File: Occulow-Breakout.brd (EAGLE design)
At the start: 50.8 x 50.8 mm, 18 parts

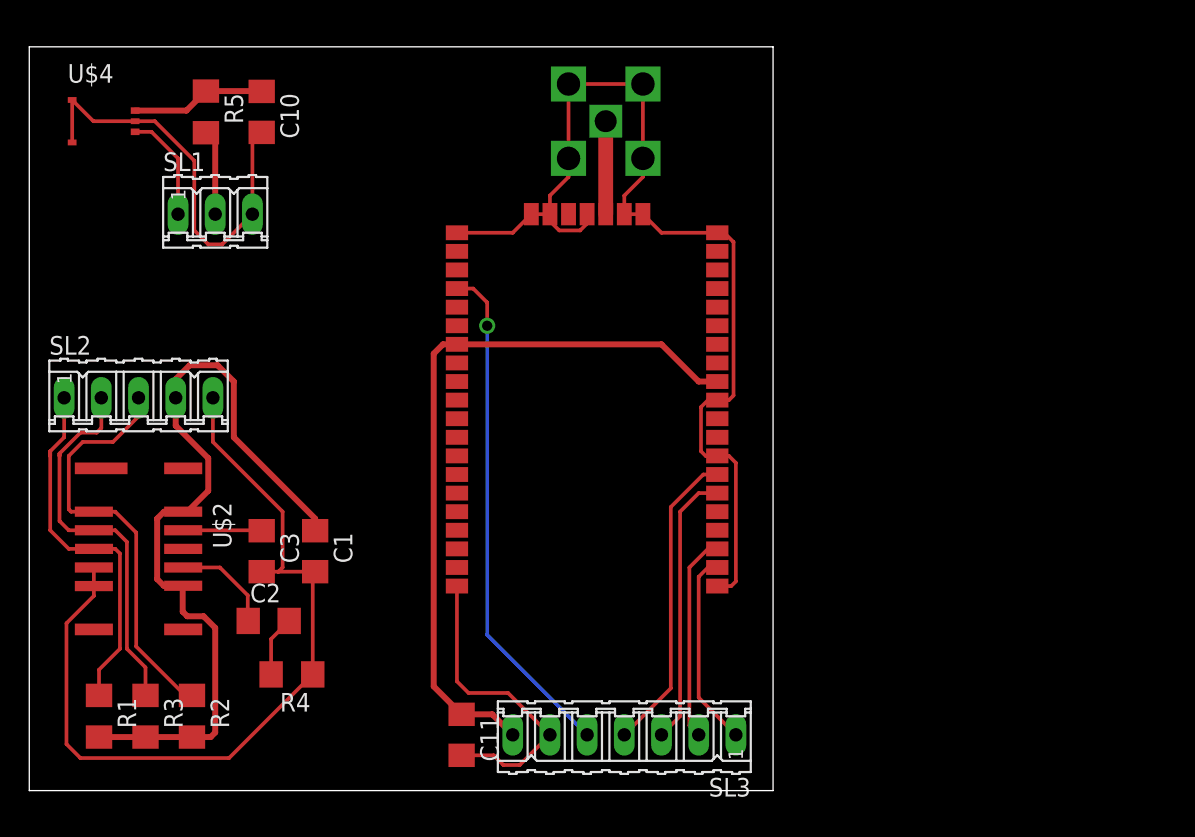
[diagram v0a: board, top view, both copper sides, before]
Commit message: Re-named ground for each module
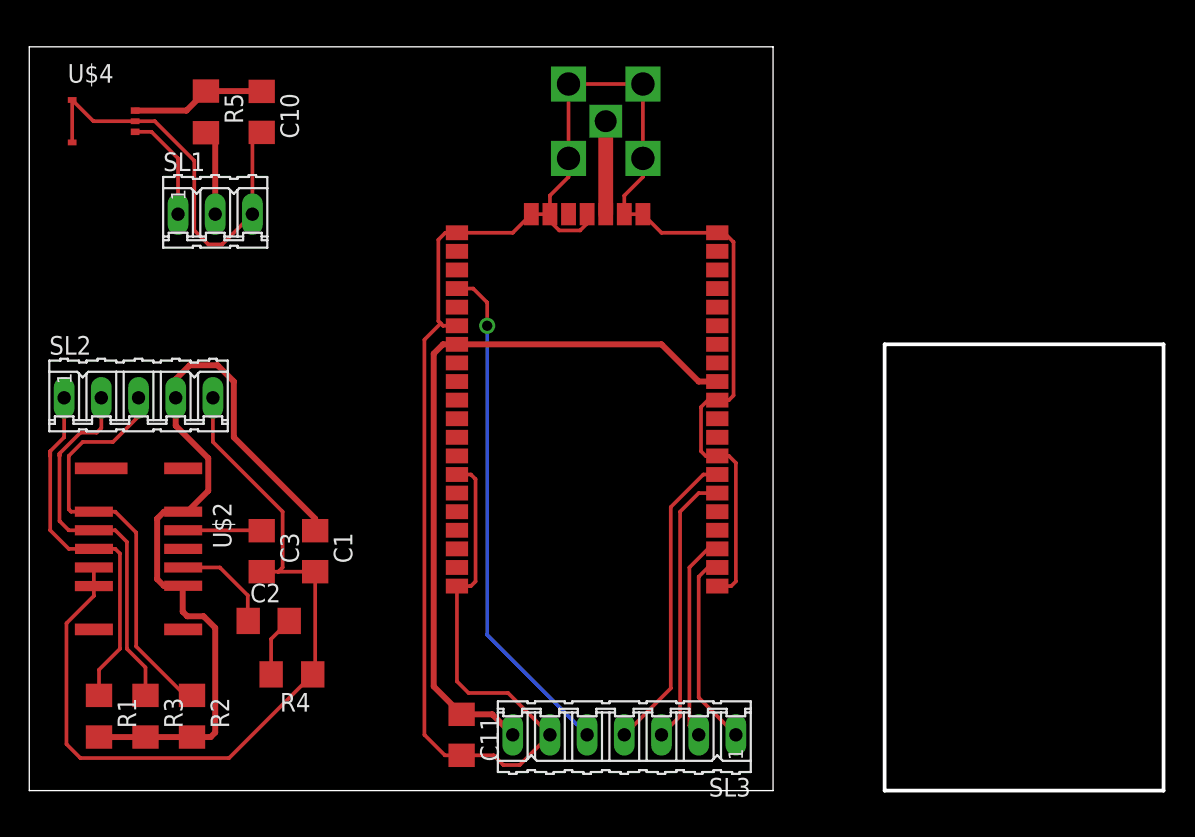
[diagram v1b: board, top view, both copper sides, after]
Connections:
- removed net GND: C1.2, C10.2, C11.2, C3.2, R4.1, SL1.3, SL2.5, SL3.6, U$1.1, U$1.11, U$1.20, U$1.21, U$1.22, U$1.24, U$1.26, U$1.27, U$1.28, U$1.33, U$1.41, U$1.47, U$1.8, U$2.5, U$2.6, U$3.1, U$3.2, U$3.3, U$3.4, U$4.2, U$4.4, U$4.5
- new net GR_GND: C1.2, C3.2, R4.1, SL2.5, U$2.5, U$2.6
- new net LR_GND: C11.2, SL3.6, U$1.1, U$1.11, U$1.20, U$1.21, U$1.22, U$1.24, U$1.26, U$1.27, U$1.28, U$1.33, U$1.41, U$1.47, U$1.8, U$3.1, U$3.2, U$3.3, U$3.4
- new net PIR_GND: C10.2, SL1.3, U$4.2, U$4.4, U$4.5
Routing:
- net GND: track 178.9 -> 0.00 mm
- net LR_GND: track 0.00 -> 142.8 mm
- net GR_GND: track 0.00 -> 57.4 mm
- net PIR_GND: track 0.00 -> 28.8 mm
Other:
- board size 50.8 x 50.8 mm -> 77.5 x 50.8 mm

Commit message: Panelized layout
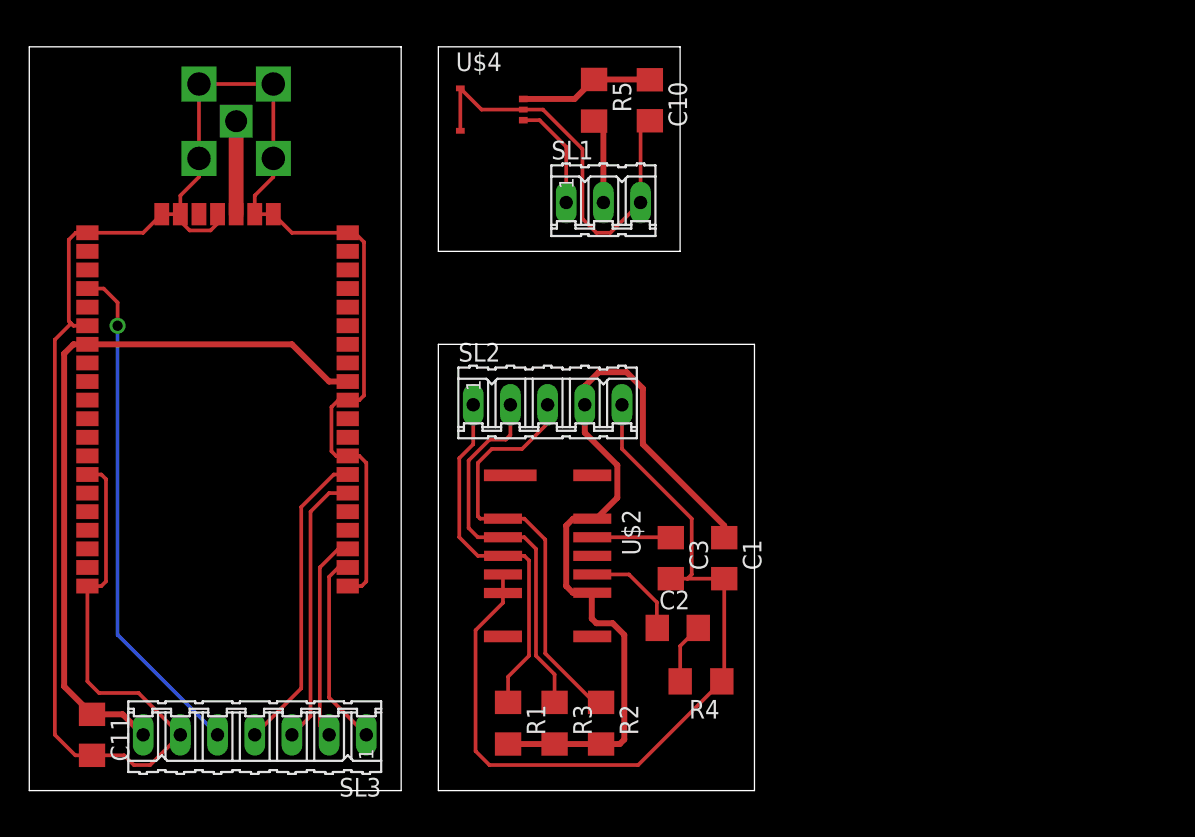
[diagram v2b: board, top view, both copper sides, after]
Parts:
- moved C1 27.9 mm to (47.5, 15.9)
- moved R1 27.9 mm to (32.7, 4.60)
- moved R2 27.9 mm to (39.1, 4.60)
- moved C2 27.9 mm to (44.3, 11.1)
- moved C3 27.9 mm to (43.8, 15.9)
- moved R3 27.9 mm to (35.9, 4.60)
- moved R4 27.9 mm to (45.9, 7.46)
- moved SL2 27.9 mm to (35.4, 26.4)
- moved U$2 27.9 mm to (35.4, 16.0)
- moved R5 26.5 mm to (38.6, 47.1)
- moved SL1 26.5 mm to (39.2, 40.2)
- moved C10 26.5 mm to (42.4, 47.1)
- moved U$4 26.5 mm to (31.6, 46.5)
- moved C11 25.2 mm to (4.29, 3.81)
- moved SL3 25.2 mm to (15.4, 3.81)
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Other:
- board size 77.5 x 50.8 mm -> 49.5 x 50.8 mm

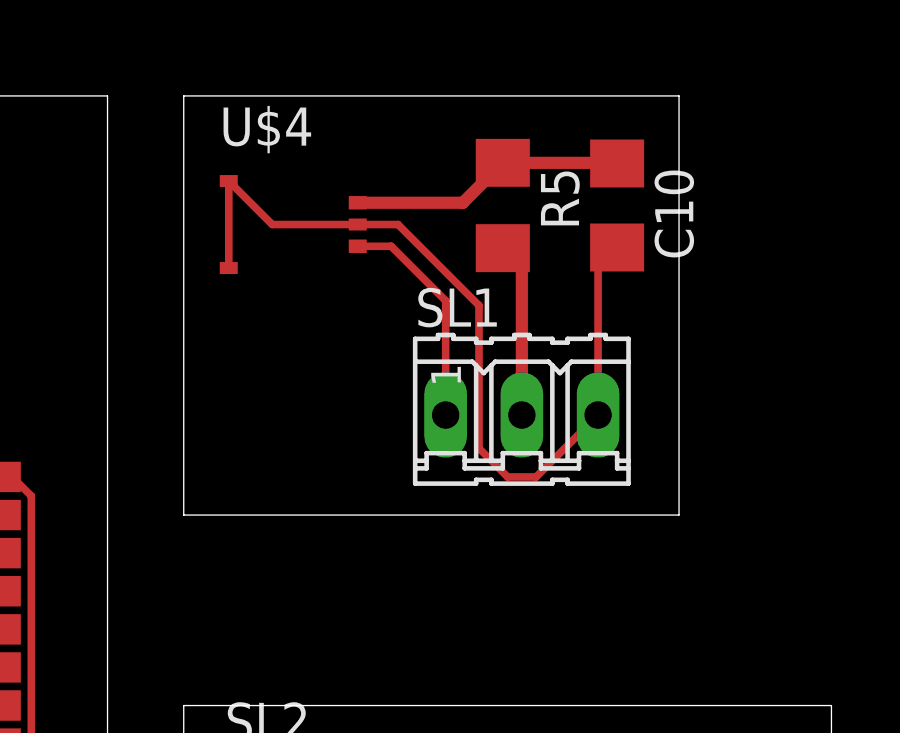
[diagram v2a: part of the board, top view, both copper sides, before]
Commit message: Labels for PIR header, rearranged
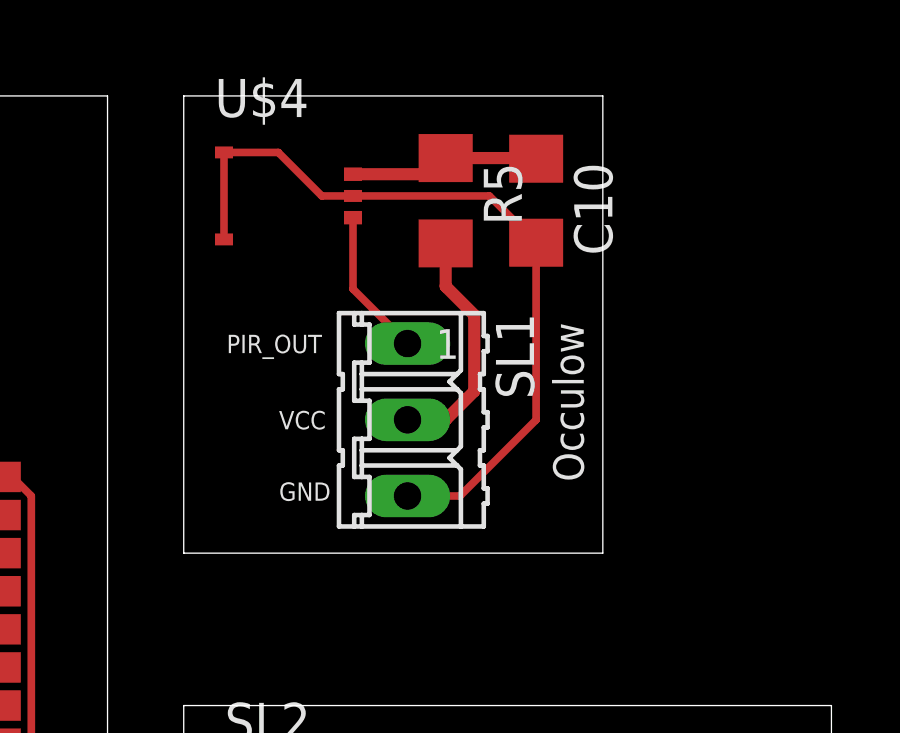
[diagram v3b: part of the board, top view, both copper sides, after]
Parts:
- moved SL1 3.81 mm to (35.4, 40.0), turned to 270 degrees
- moved C10 2.70 mm to (39.7, 47.3)
- moved R5 1.91 mm to (36.7, 47.3)
- moved U$4 0.97 mm to (31.4, 47.5)
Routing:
- net PIR_GND: track 28.8 -> 25.8 mm
- net N$5: track 9.21 -> 6.34 mm
- net PIR_OUT: track 7.49 -> 4.95 mm
- net PIR_VCC: track 5.83 -> 7.94 mm
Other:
- outline, holes or cut-outs redrawn
- board text added: "GND"
- board text added: "Occulow"
- board text added: "PIR_OUT"
- board text added: "VCC"
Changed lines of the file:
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@@
 <wire x1="49.53" y1="30.48" x2="49.53" y2="0" width="0" layer="20"/>
 <wire x1="49.53" y1="0" x2="27.94" y2="0" width="0" layer="20"/>
-<wire x1="44.45" y1="50.8" x2="44.45" y2="36.83" width="0" layer="20"/>
-<wire x1="44.45" y1="36.83" x2="27.94" y2="36.83" width="0" layer="20"/>
-<wire x1="27.94" y1="36.83" x2="27.94" y2="50.8" width="0" layer="20"/>
-<wire x1="27.94" y1="50.8" x2="44.45" y2="50.8" width="0" layer="20"/>
+<wire x1="41.91" y1="50.8" x2="41.91" y2="35.56" width="0" layer="20"/>
+<wire x1="41.91" y1="35.56" x2="27.94" y2="35.56" width="0" layer="20"/>
+<wire x1="27.94" y1="35.56" x2="27.94" y2="50.8" width="0" layer="20"/>
+<wire x1="27.94" y1="50.8" x2="41.91" y2="50.8" width="0" layer="20"/>
 <wire x1="0" y1="0" x2="0" y2="50.8" width="0" layer="20"/>
 <wire x1="0" y1="50.8" x2="25.4" y2="50.8" width="0" layer="20"/>
 <wire x1="25.4" y1="50.8" x2="25.4" y2="0" width="0" layer="20"/>
 <wire x1="25.4" y1="0" x2="0" y2="0" width="0" layer="20"/>
+<text x="29.36875" y="42.2275" size="0.6096" layer="21">PIR_OUT</text>
+<text x="31.115" y="39.6875" size="0.6096" layer="21">VCC</text>
+<text x="31.115" y="37.30625" size="0.6096" layer="21">GND</text>
+<text x="41.275" y="37.94125" size="1.016" layer="21" rot="R90">Occulow</text>
 </plain>
 <attributes>
@@
 <element name="U$2" library="GridEye" package="AMG8833" value="AMG8833SMD" x="35.40125" y="16.03375" rot="R270"/>
 <element name="U$3" library="SMA-JACK" package="SMA-JACK" value="SMA-JACKFEMALE" x="14.12875" y="45.72"/>
-<element name="U$4" library="PIR" package="IRS-B210ST01" value="IRS-B210ST01" x="31.59125" y="46.51375"/>
-<element name="C10" library="rcl" package="C1206" value="100uF" x="42.38625" y="47.14875" rot="R270"/>
-<element name="R5" library="resistor" package="R1206" value="619k" x="38.57625" y="47.14875" rot="R270"/>
+<element name="U$4" library="PIR" package="IRS-B210ST01" value="IRS-B210ST01" x="31.4325" y="47.46625"/>
+<element name="C10" library="rcl" package="C1206" value="100uF" x="39.6875" y="47.3075" rot="R270"/>
+<element name="R5" library="resistor" package="R1206" value="619k" x="36.67125" y="47.3075" rot="R270"/>
 <element name="C11" library="rcl" package="C1206" value="10uF" x="4.28625" y="3.81" rot="R270"/>
-<element name="SL1" library="con-amp-quick" package="03P" value="" x="39.21125" y="40.16375">
-<attribute name="MF" value="" x="39.21125" y="40.16375" size="1.778" layer="27" display="off"/>
-<attribute name="OC_FARNELL" value="unknown" x="39.21125" y="40.16375" size="1.778" layer="27" display="off"/>
-<attribute name="OC_NEWARK" value="unknown" x="39.21125" y="40.16375" size="1.778" layer="27" display="off"/>
-<attribute name="MPN" value="" x="39.21125" y="40.16375" size="1.778" layer="27" display="off"/>
+<element name="SL1" library="con-amp-quick" package="03P" value="" x="35.40125" y="40.005" rot="R270">
+<attribute name="MF" value="" x="35.40125" y="40.005" size="1.778" layer="27" rot="R270" display="off"/>
+<attribute name="OC_FARNELL" value="unknown" x="35.40125" y="40.005" size="1.778" layer="27" rot="R270" display="off"/>
+<attribute name="OC_NEWARK" value="unknown" x="35.40125" y="40.005" size="1.778" layer="27" rot="R270" display="off"/>
+<attribute name="MPN" value="" x="35.40125" y="40.005" size="1.778" layer="27" rot="R270" display="off"/>
 </element>
 <element name="SL2" library="con-amp-quick" package="05P" value="" x="35.40125" y="26.3525">
@@
 <contactref element="C10" pad="1"/>
 <contactref element="R5" pad="1"/>
-<wire x1="33.74125" y1="47.23875" x2="37.24425" y2="47.23875" width="0.4064" layer="1"/>
-<wire x1="37.24425" y1="47.23875" x2="38.57625" y2="48.57075" width="0.4064" layer="1"/>
-<wire x1="38.57625" y1="48.57075" x2="42.36425" y2="48.57075" width="0.4064" layer="1"/>
-<wire x1="42.36425" y1="48.57075" x2="42.38625" y2="48.54875" width="0.4064" layer="1"/>
+<wire x1="33.5825" y1="48.19125" x2="36.133" y2="48.19125" width="0.4064" layer="1"/>
+<wire x1="36.133" y1="48.19125" x2="36.67125" y2="48.7295" width="0.4064" layer="1"/>
+<wire x1="36.67125" y1="48.7295" x2="39.6655" y2="48.7295" width="0.4064" layer="1"/>
+<wire x1="39.6655" y1="48.7295" x2="39.6875" y2="48.7075" width="0.4064" layer="1"/>
 </signal>
 <signal name="PIR_OUT">
 <contactref element="U$4" pad="1"/>
 <contactref element="SL1" pad="1"/>
-<wire x1="33.74125" y1="45.78875" x2="34.85625" y2="45.78875" width="0.254" layer="1"/>
-<wire x1="34.85625" y1="45.78875" x2="36.67125" y2="43.97375" width="0.254" layer="1"/>
-<wire x1="36.67125" y1="43.97375" x2="36.67125" y2="40.16375" width="0.254" layer="1"/>
+<wire x1="33.5825" y1="46.74125" x2="33.5825" y2="44.36375" width="0.254" layer="1"/>
+<wire x1="33.5825" y1="44.36375" x2="35.40125" y2="42.545" width="0.254" layer="1"/>
 </signal>
 <signal name="GR_VCC">
@@
 <contactref element="R5" pad="2"/>
 <contactref element="SL1" pad="2"/>
-<wire x1="39.21125" y1="40.16375" x2="39.21125" y2="45.09175" width="0.4064" layer="1"/>
-<wire x1="39.21125" y1="45.09175" x2="38.57625" y2="45.72675" width="0.4064" layer="1"/>
+<wire x1="36.67125" y1="45.8855" x2="36.67125" y2="44.45" width="0.4064" layer="1"/>
+<wire x1="36.67125" y1="44.45" x2="37.62375" y2="43.4975" width="0.4064" layer="1"/>
+<wire x1="37.62375" y1="43.4975" x2="37.62375" y2="40.9575" width="0.4064" layer="1"/>
+<wire x1="37.62375" y1="40.9575" x2="36.67125" y2="40.005" width="0.4064" layer="1"/>
+<wire x1="36.67125" y1="40.005" x2="35.40125" y2="40.005" width="0.4064" layer="1"/>
 </signal>
 <signal name="LR_VCC">
@@
 <contactref element="U$4" pad="4"/>
 <contactref element="U$4" pad="5"/>
-<wire x1="29.44125" y1="47.96375" x2="29.44125" y2="45.06375" width="0.254" layer="1"/>
 <contactref element="U$4" pad="2"/>
 <contactref element="C10" pad="2"/>
-<wire x1="30.89125" y1="46.51375" x2="33.74125" y2="46.51375" width="0.254" layer="1"/>
 <contactref element="SL1" pad="3"/>
-<wire x1="35.08375" y1="46.51375" x2="37.7825" y2="43.815" width="0.254" layer="1"/>
-<wire x1="37.7825" y1="43.815" x2="37.7825" y2="39.0525" width="0.254" layer="1"/>
-<wire x1="37.7825" y1="39.0525" x2="38.735" y2="38.1" width="0.254" layer="1"/>
-<wire x1="38.735" y1="38.1" x2="39.6875" y2="38.1" width="0.254" layer="1"/>
-<wire x1="39.6875" y1="38.1" x2="41.75125" y2="40.16375" width="0.254" layer="1"/>
-<wire x1="41.75125" y1="45.11375" x2="41.75125" y2="40.16375" width="0.254" layer="1"/>
-<wire x1="30.89125" y1="46.51375" x2="29.44125" y2="47.96375" width="0.254" layer="1"/>
-<wire x1="33.74125" y1="46.51375" x2="35.08375" y2="46.51375" width="0.254" layer="1"/>
-<wire x1="42.38625" y1="45.74875" x2="41.75125" y2="45.11375" width="0.254" layer="1"/>
+<wire x1="29.2825" y1="46.01625" x2="29.2825" y2="48.91625" width="0.254" layer="1"/>
+<wire x1="29.2825" y1="48.91625" x2="31.09375" y2="48.91625" width="0.254" layer="1"/>
+<wire x1="31.09375" y1="48.91625" x2="32.54375" y2="47.46625" width="0.254" layer="1"/>
+<wire x1="32.54375" y1="47.46625" x2="33.5825" y2="47.46625" width="0.254" layer="1"/>
+<wire x1="39.6875" y1="45.9075" x2="39.6875" y2="40.005" width="0.254" layer="1"/>
+<wire x1="39.6875" y1="40.005" x2="37.1475" y2="37.465" width="0.254" layer="1"/>
+<wire x1="37.1475" y1="37.465" x2="35.40125" y2="37.465" width="0.254" layer="1"/>
+<wire x1="33.5825" y1="47.46625" x2="38.12875" y2="47.46625" width="0.254" layer="1"/>
+<wire x1="38.12875" y1="47.46625" x2="39.6875" y2="45.9075" width="0.254" layer="1"/>
 </signal>
 <signal name="LR_GND">
